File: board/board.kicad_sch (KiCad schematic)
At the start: 22 parts

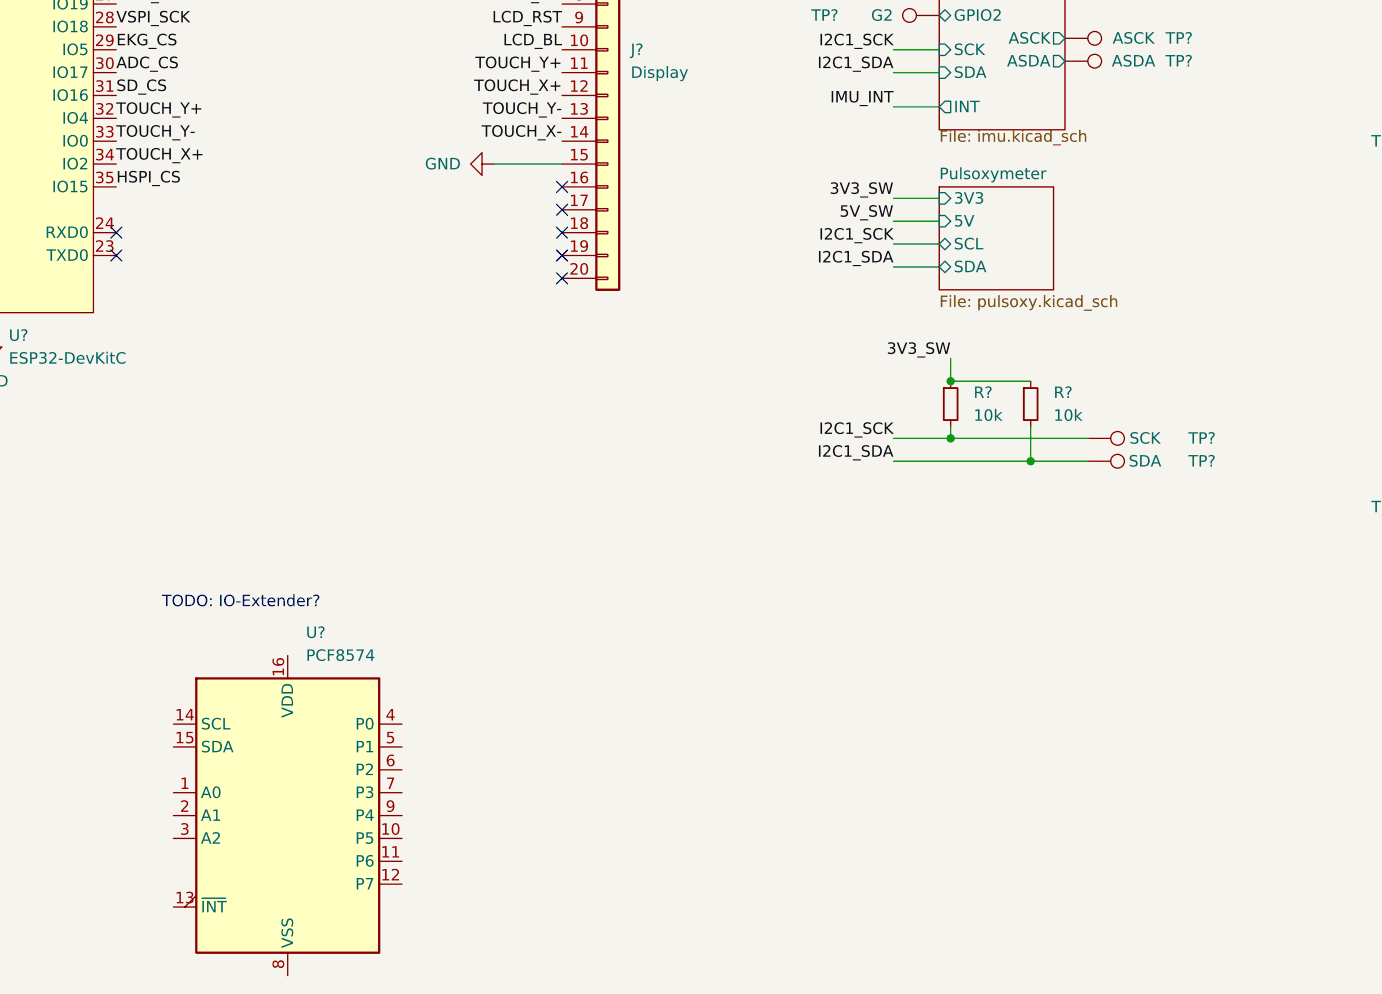
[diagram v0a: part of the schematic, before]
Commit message: added io expander
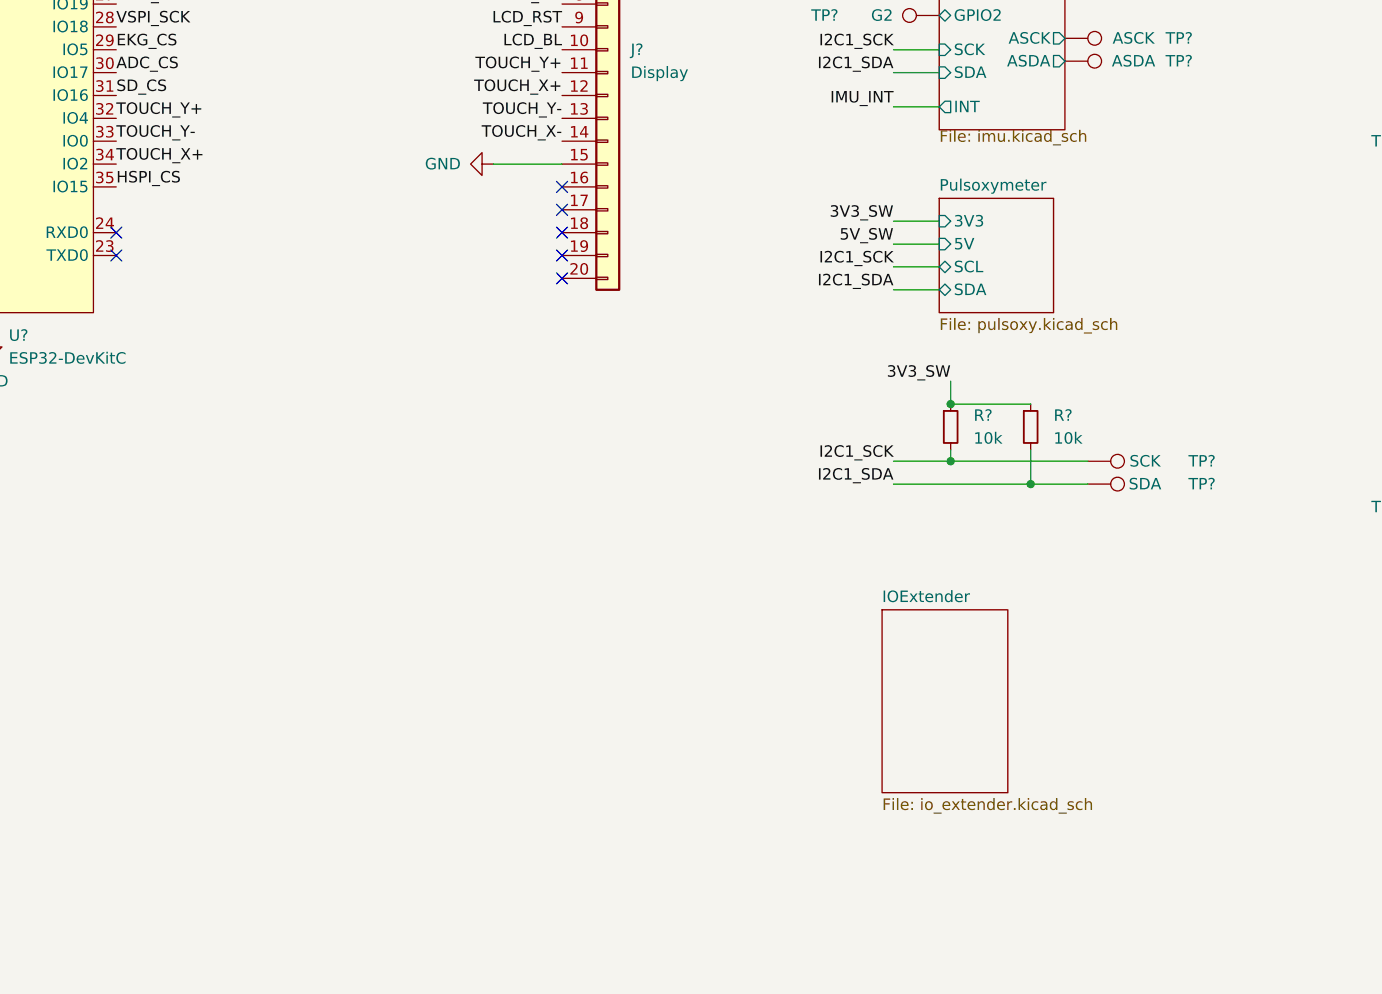
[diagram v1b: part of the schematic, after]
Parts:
- removed U?: PCF8574, symbol Interface_Expansion:PCF8574
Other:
- added sheet IOExtender (io_extender.kicad_sch)
- note removed: "TODO: IO-Extender?"
- moved on the sheet: R?, TP?

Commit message: updated after meeting
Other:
- note added: "TODO: RTC? BOB? Clock: 2,048 MHz (EKG und ADC)"
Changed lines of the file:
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@@
     (stroke (width 0) (type default) (color 0 0 0 0))
+  )
+  (text "TODO:\nRTC? BOB?\nClock: 2,048 MHz (EKG und ADC)" (at 96.52 96.52 0)
+    (effects (font (size 1.27 1.27)) (justify left bottom))
   )
   (label "I2C1_SCK" (at 147.32 87.63 180)

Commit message: ERC run
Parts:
- added R3, R4: 30R, symbol Device:R_Small
- added X1: XO32, Oscillator:Oscillator_SMD_EuroQuartz_XO32-4Pin_3.2x2.5mm, symbol Oscillator:XO32
- J1: renamed from J?; symbol Connector_Generic:Conn_01x20 -> Connector_Generic:Conn_01x15
- gave numbers to parts that had none: 20
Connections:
- net +3V3: now also X1.4 (V+)
- net GND: now also X1.2 (GND)
- new net ADC/MCLK: R4.1
- new net EKG/MCLK: R3.1
- new net MCLK: R3.2, R4.2, X1.3 (OUT)
- no-connect marks 15 -> 12
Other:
- added sheet BreadBoard (breadboard.kicad_sch)
- sheet ADC ports: added MCLK; removed none
- sheet EKG ports: added MCLK; removed none
- sheet IOExtender ports: added 3V3, P0, P1, P2, P3, P4, P5, P6, P7, SCL, SDA, ~{INT}; removed none
- note removed: "TODO: RTC? BOB? Clock: 2,048 MHz (EKG und ADC)"
- moved on the sheet: TP13, TP14, TP15, TP16, TP17

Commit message: updated schematic after review
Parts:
- added H? (x5): MountingHole, symbol Mechanical:MountingHole
- R1, R2: value 10k -> 2k2
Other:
- note added: "Mark default position of jumpers in layout"
- note added: "TODO: Caps"
- moved on the sheet: X1

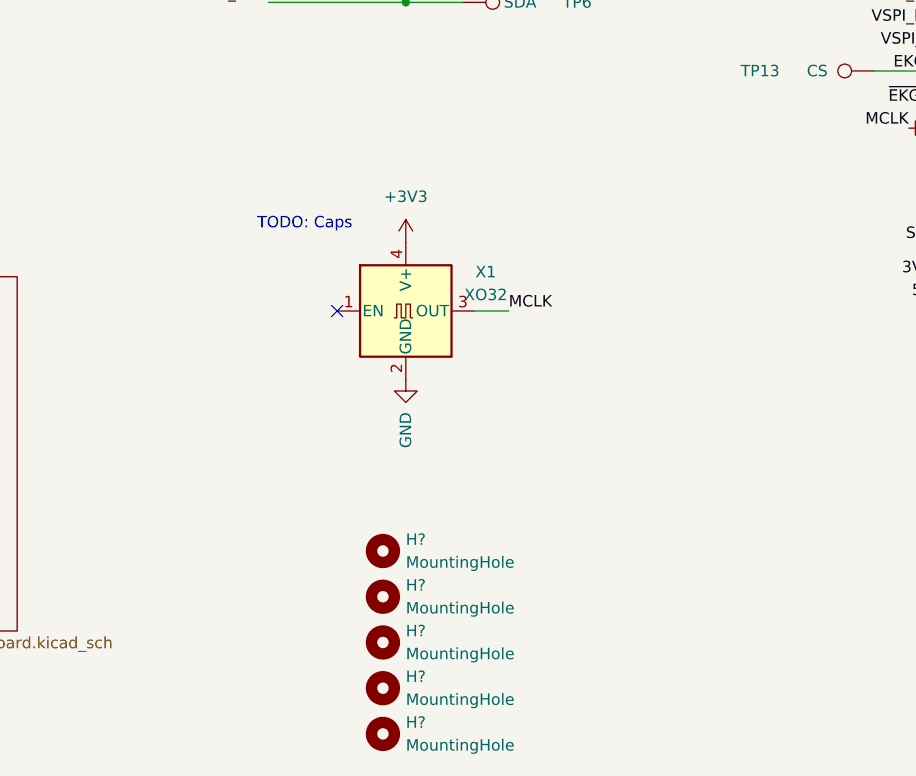
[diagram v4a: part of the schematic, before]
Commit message: added fuse and capacitor to schematic
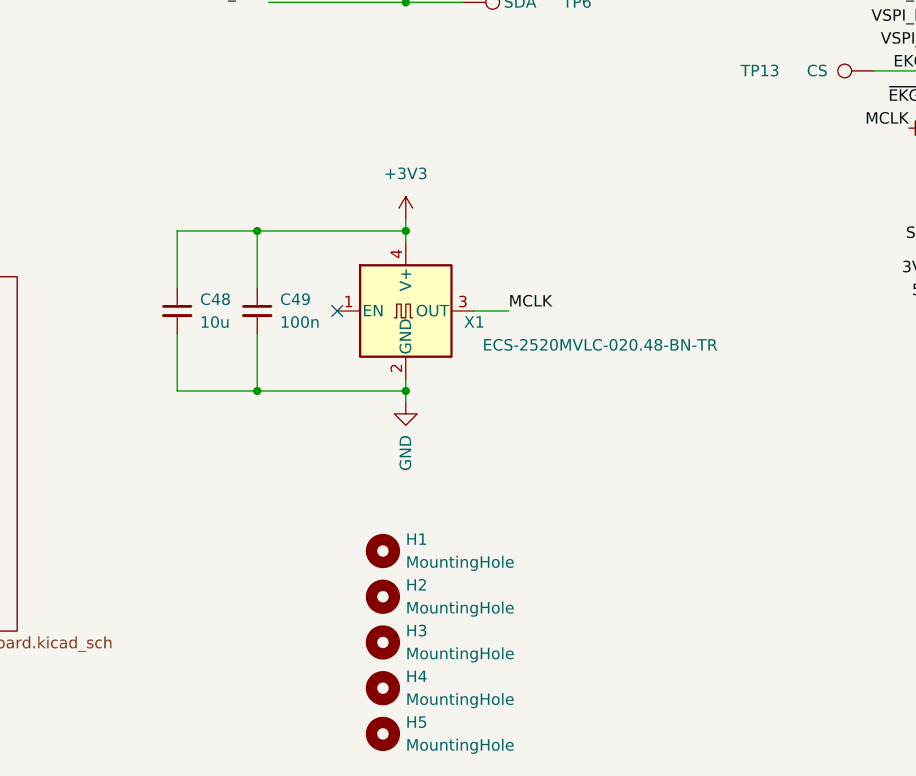
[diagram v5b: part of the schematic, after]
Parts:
- added C48: 10u, symbol Device:C_Small
- added C49: 100n, symbol Device:C_Small
- X1: value XO32 -> ECS-2520MVLC-020.48-BN-TR
- gave numbers to parts that had none: 5
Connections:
- net +3V3: now also C48.1, C49.1
- net GND: now also C48.2, C49.2
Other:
- note removed: "TODO: Caps"

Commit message: added footprints to symbols and started layout
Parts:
- C48: footprint (none) -> Capacitor_SMD:C_0603_1608Metric
- C49: footprint (none) -> Capacitor_SMD:C_0402_1005Metric
- H1, H2, H3, H4, H5: footprint (none) -> ownLib:MountingHole_3.2mm_M3_no_Mask
- J1: footprint (none) -> Connector_PinHeader_2.54mm:PinHeader_1x15_P2.54mm_Vertical
- R1, R2, R3, R4: footprint (none) -> Resistor_SMD:R_0402_1005Metric
- TP1, TP10, TP11, TP12, TP13, TP14, TP15, TP16, TP17, TP2, TP3, TP4, TP5, TP6, TP7, TP8, TP9: footprint (none) -> TestPoint:TestPoint_Pad_D1.0mm
- U1: footprint (none) -> ownLib:ESP32-DevKitC

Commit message: WIP pushed for meeting
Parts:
- removed H1, H2, H3, H4, H5: MountingHole, ownLib:MountingHole_3.2mm_M3_no_Mask, symbol Mechanical:MountingHole
- removed J1: Display, Connector_PinHeader_2.54mm:PinHeader_1x15_P2.54mm_Vertical, symbol Connector_Generic:Conn_01x15
- added TP18: MCLK, TestPoint:TestPoint_Pad_D1.0mm, symbol Connector:TestPoint
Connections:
- net TOUCH_X- is gone; now on net SIG_SW: U1.11 (IO27)
- net TOUCH_Y+ is gone; now on net ~{EKGReset}: U1.32 (IO4)
- net TOUCH_Y- is gone; now on net ~{EKGPowerDown}: U1.33 (IO0)
- net LCD_BL: now also U1.8 (IO33)
- net LCD_DC: now also U1.9 (IO25)
- net LCD_RST: now also U1.10 (IO26)
- net MCLK: now also TP18.1
- net SIG_SW: no longer U1.10 (IO26)
- net ~{EKGPowerDown}: no longer U1.9 (IO25)
- net ~{EKGReset}: no longer U1.8 (IO33)
- net TOUCH_X+ renamed ~{DISPLAY_IRQ}
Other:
- added sheet Display (display.kicad_sch)

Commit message: finished layout for review
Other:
- sheet SD card ports: added CardDet; removed none
- moved on the sheet: TP7, TP8
